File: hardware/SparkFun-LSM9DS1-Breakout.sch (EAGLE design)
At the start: 27 parts, among them U1 LSM9DS1

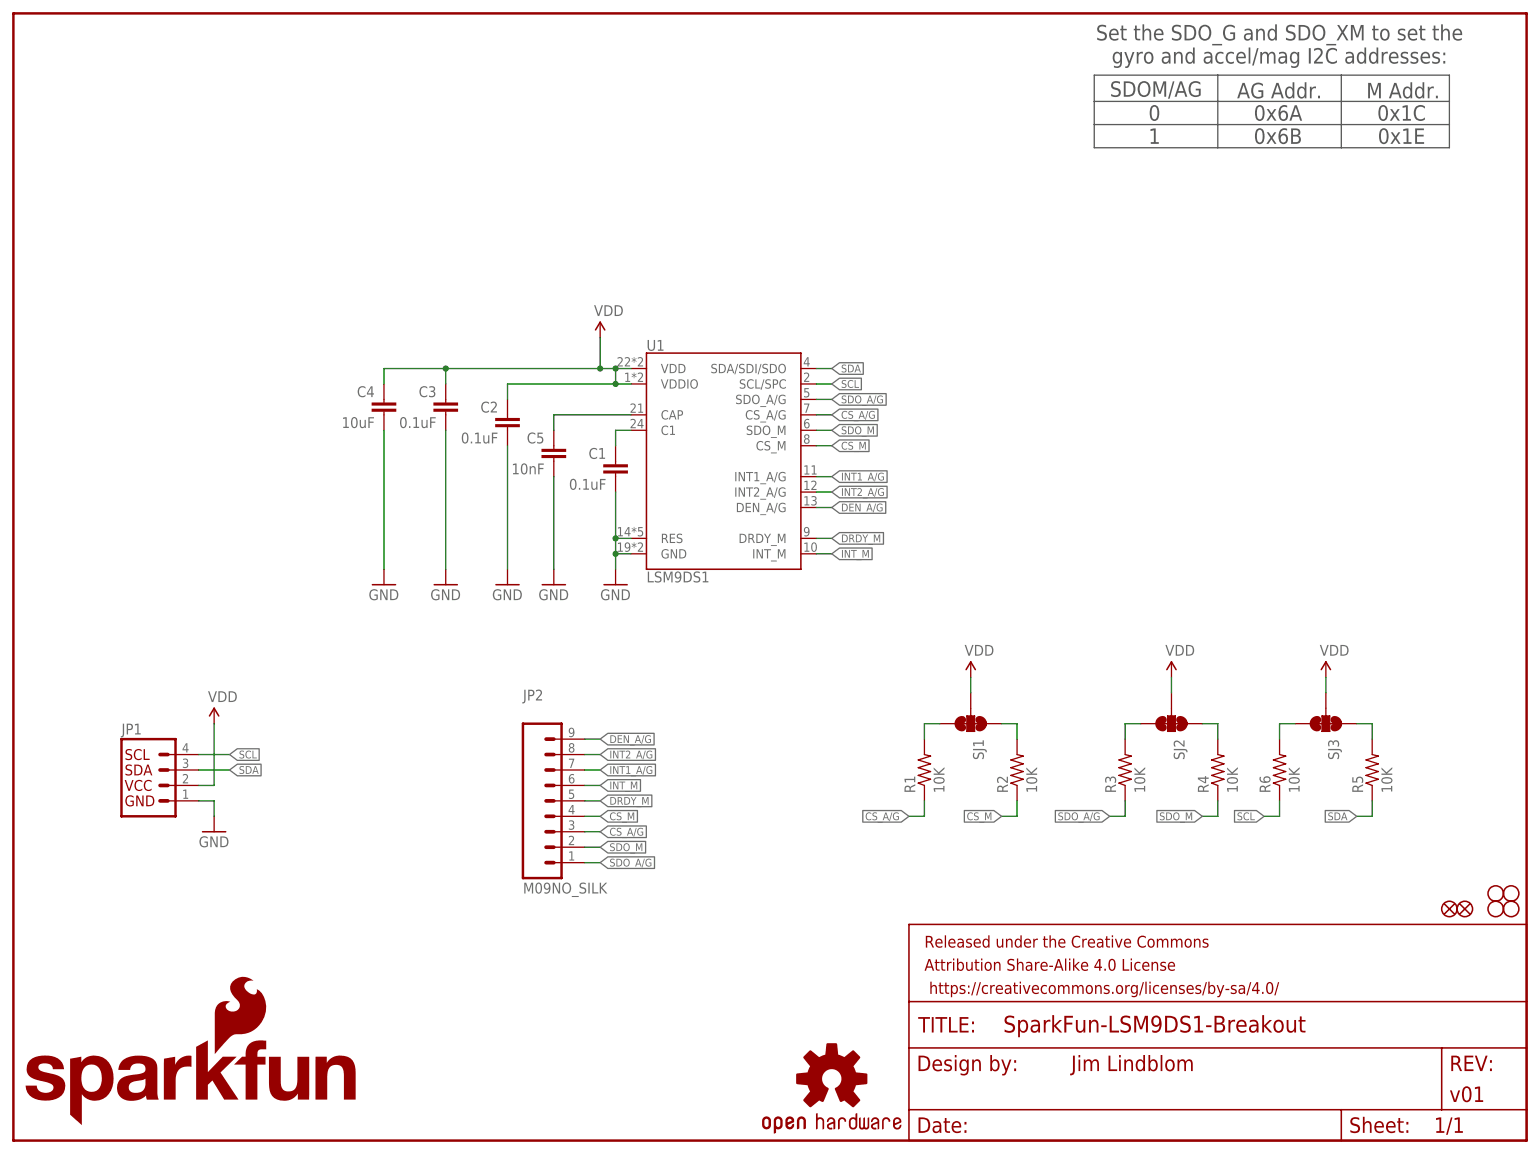
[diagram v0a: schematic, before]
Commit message: Cleaning up schematic.
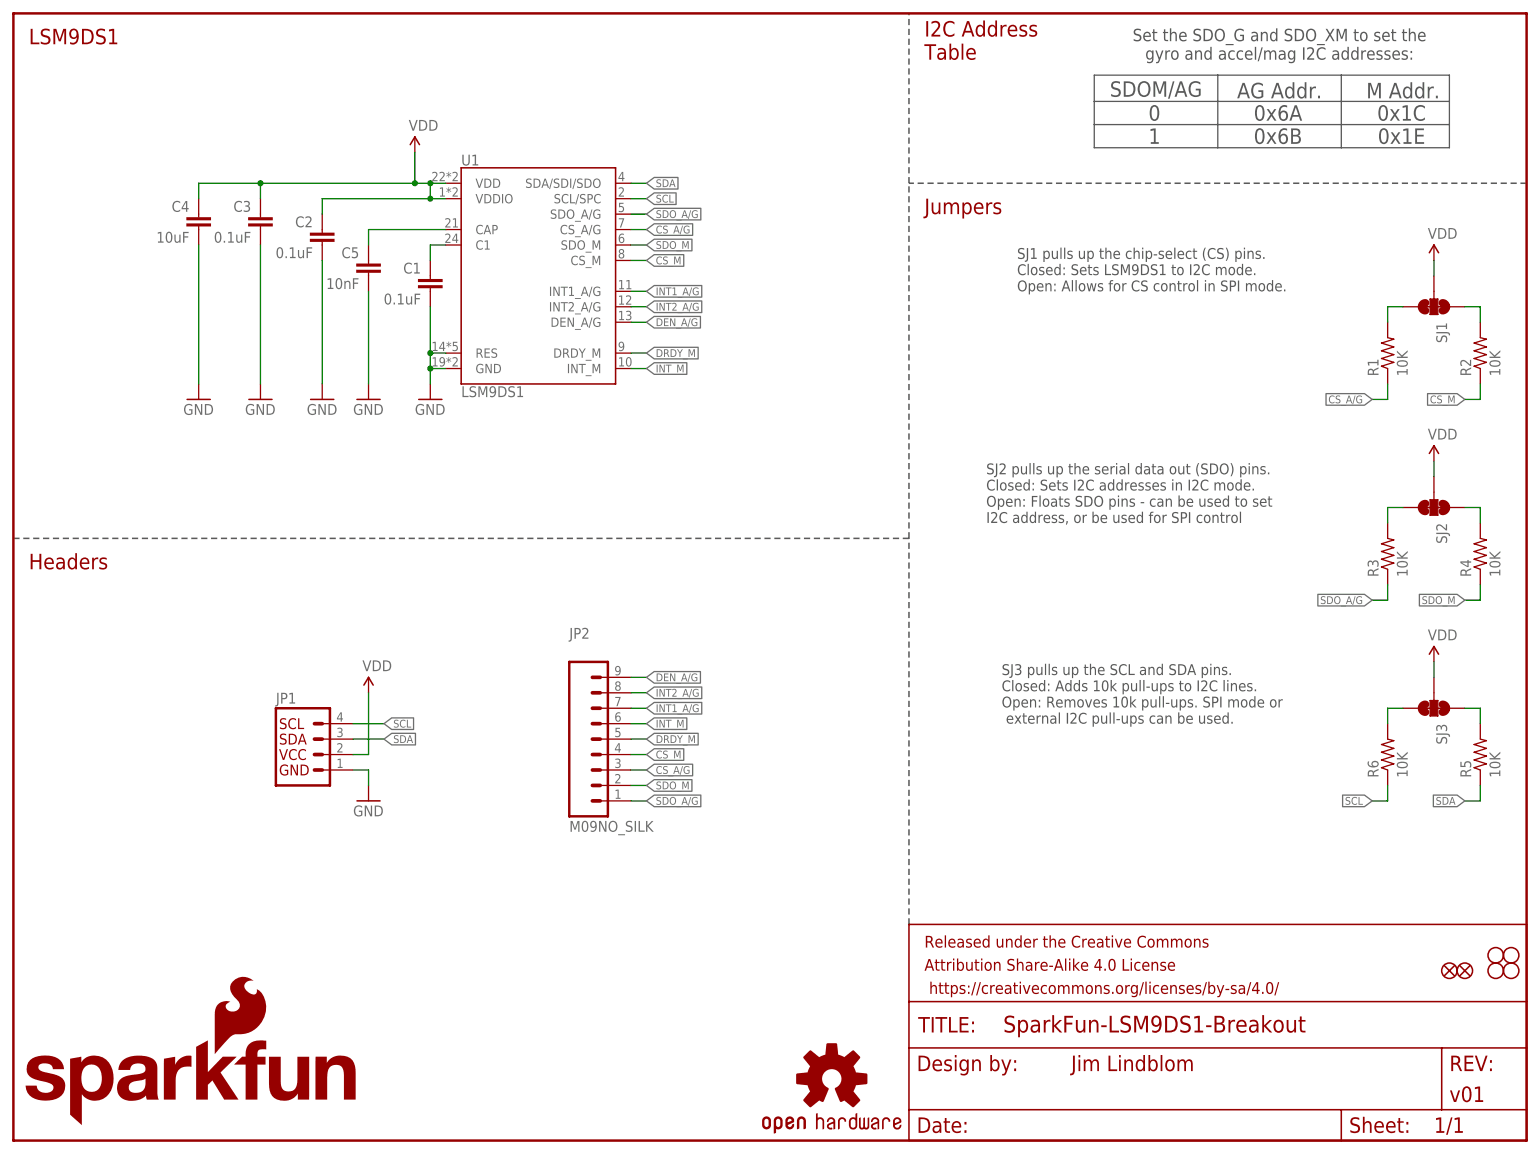
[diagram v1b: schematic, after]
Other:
- note added: "Headers"
- note added: "I2C Address Table"
- note added: "Jumpers"
- note added: "LSM9DS1"
- note added: "SJ1 pulls up the chip-select (CS) pins. Closed: Sets LSM9DS1 to I2C mode. Open: Allows for CS control in SPI mode."
- note added: "SJ2 pulls up the serial data out (SDO) pins. Closed: Sets I2C addresses in I2C mode. Open: Floats SDO pins - can be used to set I2C address, or be used for SPI control"
- note added: "SJ3 pulls up the SCL and SDA pins. Closed: Adds 10k pull-ups to I2C lines. Open: Removes 10k pull-ups. SPI mode or external I2C pull-ups can be used."
- moved on the sheet: C1, C2, C3, C4, C5, JP1, JP2, R1, R2, R3, R4, R5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

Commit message: Adding board mesurements, fixing some traces, labelling VCC range.
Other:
- note added: "VDD Range: 1.9-3.6V"
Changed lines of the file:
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@@
 <text x="2.54" y="180.34" size="2.54" layer="94">LSM9DS1</text>
 <text x="2.54" y="93.98" size="2.54" layer="94">Headers</text>
+<text x="38.1" y="81.28" size="2.54" layer="97">VDD Range: 1.9-3.6V</text>
 </plain>
 <instances>

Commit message: Re-arranging some silk. Updating board to v10.
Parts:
- FRAME1: VERSION (none) -> v10
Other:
- note added: "Set the SDO_AG and SDO_M to set the accel/gryo and mag I2C addresses:"
- note removed: "Set the SDO_G and SDO_XM to set the gyro and accel/mag I2C addresses:"
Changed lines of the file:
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@@
 <part name="FRAME1" library="SparkFun-Aesthetics" deviceset="FRAME-LETTER" device="">
 <attribute name="DESIGNER" value="Jim Lindblom"/>
+<attribute name="VERSION" value="v10"/>
 </part>
 <part name="U1" library="LSM9DS1_temp" deviceset="LSM9DS1" device=""/>
@@
 <text x="208.026" y="167.132" size="2.54" layer="97" align="center">0x6A
 0x6B</text>
-<text x="208.28" y="180.34" size="2.032" layer="97" align="center">Set the SDO_G and SDO_XM to set the
-gyro and accel/mag I2C addresses:</text>
+<text x="208.28" y="180.34" size="2.032" layer="97" align="center">Set the SDO_AG and SDO_M to set the
+accel/gryo and mag I2C addresses:</text>
 <text x="165.1" y="139.7" size="1.778" layer="97">SJ1 pulls up the chip-select (CS) pins.
 Closed: Sets LSM9DS1 to I2C mode.
